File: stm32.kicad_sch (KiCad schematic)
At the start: 33 parts, among them J1 TC2030, SW1 SW_Push, U1 STM32F411CEUx, U2 BMI088, U3 BMP388, U4 W25Q128JVSIQ, Y1 Crystal_GND24

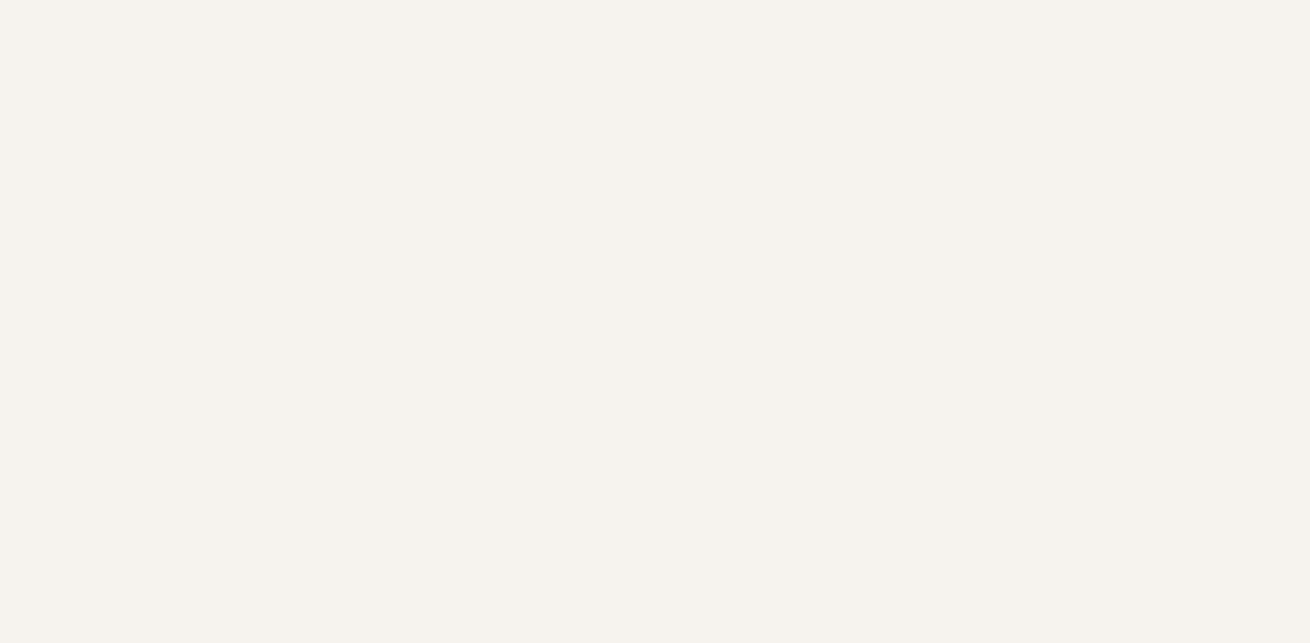
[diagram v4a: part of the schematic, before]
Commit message: Power: TP4056 charger (Iprog=255mA via 4.7k PROG, status LEDs, NTC disabled)
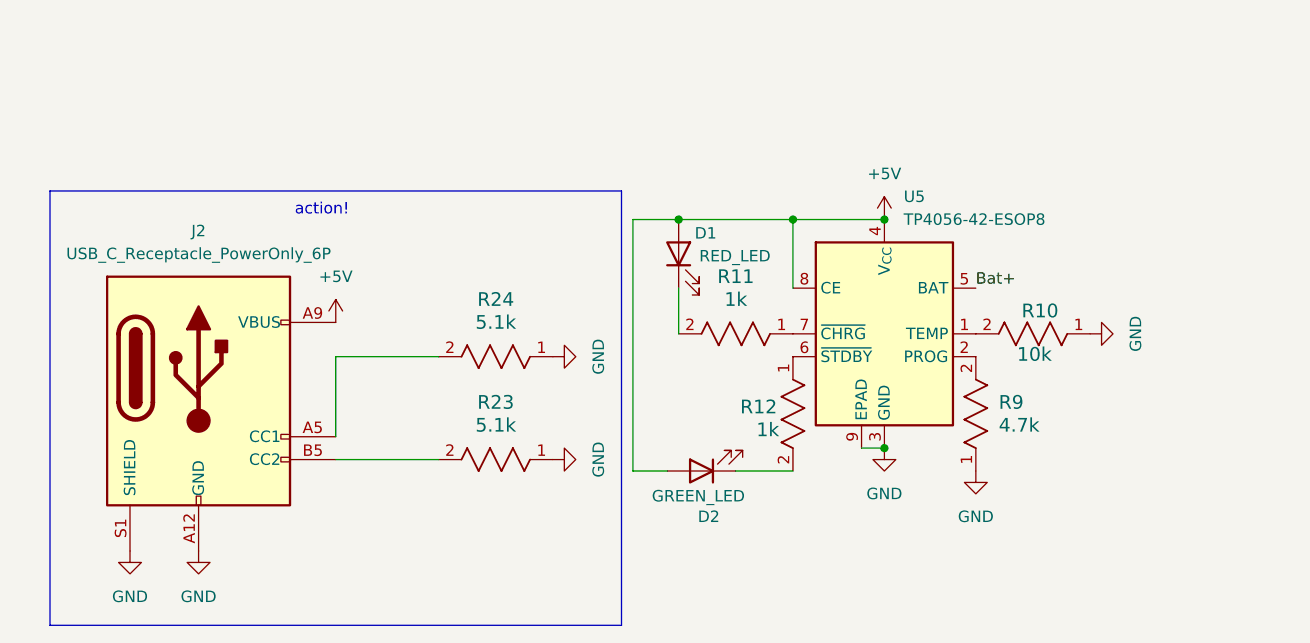
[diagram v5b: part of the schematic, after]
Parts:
- added D1: RED_LED, symbol Device:LED
- added D2: GREEN_LED, symbol Device:LED
- added J2: USB_C_Receptacle_PowerOnly_6P, Connector_USB:USB_C_Receptacle_GCT_USB4125-xx-x_6P_TopMnt_Horizontal, symbol Connector:USB_C_Receptacle_PowerOnly_6P
- added R10: 10k, 240Library:STA_CF14_STP, symbol 240Library:CF14JT1K00
- added R11, R12: 1k, 240Library:STA_CF14_STP, symbol 240Library:CF14JT1K00
- added R23, R24: 5.1k, 240Library:STA_CF14_STP, symbol 240Library:CF14JT1K00
- added R9: 4.7k, 240Library:STA_CF14_STP, symbol 240Library:CF14JT1K00
- added U5: TP4056-42-ESOP8, Package_SO:SOIC-8-1EP_3.9x4.9mm_P1.27mm_EP2.41x3.3mm_ThermalVias, symbol Battery_Management:TP4056-42-ESOP8
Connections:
- net GND: now also J2.A12 (GND), J2.B12 (GND), J2.S1 (SHIELD), R10.1, R23.1, R24.1, R9.1, U5.3 (GND), U5.9 (EPAD)
- new net: R10.2, U5.1 (TEMP)
- new net: R9.2, U5.2 (PROG)
- new net: R12.1, U5.6 (~{STDBY})
- new net: R11.1, U5.7 (~{CHRG})
- new net: D1.1 (K), R11.2
- new net: J2.A5 (CC1), R24.2
- new net: D2.1 (K), R12.2
- new net: J2.B5 (CC2), R23.2
- new net +5V: D1.2 (A), D2.2 (A), J2.A9 (VBUS), J2.B9 (VBUS), U5.4 (V_{CC}), U5.8 (CE)
- new net Bat+: U5.5 (BAT)
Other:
- note added: "action!"

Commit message: small update
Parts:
- added U6: AP63203WU, Package_TO_SOT_SMD:TSOT-23-6, symbol Regulator_Switching:AP63203WU
- R10, R11, R12, R23, R24, R9: footprint 240Library:STA_CF14_STP -> Resistor_SMD:R_0402_1005Metric
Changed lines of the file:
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@@
 	)
 	(symbol
+		(lib_id "Regulator_Switching:AP63203WU")
+		(at 180.34 123.19 0)
+		(unit 1)
+		(exclude_from_sim no)
+		(in_bom yes)
+		(on_board yes)
+		(dnp no)
+		(fields_autoplaced yes)
+		(property "Reference" "U6"
+			(at 180.34 113.03 0)
+			(effects
+				(font
+					(size 1.27 1.27)
+				)
+			)
+		)
+		(property "Value" "AP63203WU"
+			(at 180.34 115.57 0)
+			(effects
+				(font
+					(size 1.27 1.27)
+				)
+			)
+		)
+		(property "Footprint" "Package_TO_SOT_SMD:TSOT-23-6"
+			(at 180.34 146.05 0)
+			(effects
+				(font
+					(size 1.27 1.27)
+				)
+				(hide yes)
+			)
+		)
+		(property "Datasheet" "https://www.diodes.com/assets/Datasheets/AP63200-AP63201-AP63203-AP63205.pdf"
+			(at 180.34 123.19 0)
+			(effects
+				(font
+					(size 1.27 1.27)
+				)
+				(hide yes)
+			)
+		)
+		(property "Description" "2A, 1.1MHz Buck DC/DC Converter, fixed 3.3V output voltage, TSOT-23-6"
+			(at 180.34 123.19 0)
+			(effects
+				(font
+					(size 1.27 1.27)
+				)
+				(hide yes)
+			)
+		)
+		(pin "1"
+		)
+		(pin "6"
+		)
+		(pin "5"
+		)
+		(pin "4"
+		)
+		(pin "2"
+		)
+		(pin "3"
+		)
+		(instances
+			(project ""
+				(path "/807257e6-524f-404b-b91f-049b9c2bdd5b"
+					(reference "U6")
+					(unit 1)
+				)
+			)
+		)
+	)
+	(symbol
 		(lib_id "power:+5V")
 		(at 46.99 161.29 0)
@@
 			)
 		)
-		(property "Footprint" "240Library:STA_CF14_STP"
+		(property "Footprint" "Resistor_SMD:R_0402_1005Metric"
 			(at 130.81 162.56 0)
 			(effects
@@
 			)
 		)
-		(property "Footprint" "240Library:STA_CF14_STP"
+		(property "Footprint" "Resistor_SMD:R_0402_1005Metric"
 			(at 118.11 177.8 0)
 			(effects
@@
 			)
 		)
-		(property "Footprint" "240Library:STA_CF14_STP"
+		(property "Footprint" "Resistor_SMD:R_0402_1005Metric"
 			(at 97.79 162.56 0)
 			(effects
@@
 			)
 		)
-		(property "Footprint" "240Library:STA_CF14_STP"
+		(property "Footprint" "Resistor_SMD:R_0402_1005Metric"
 			(at 71.12 165.1 0)
 			(effects
@@
 			)
 		)
-		(property "Footprint" "240Library:STA_CF14_STP"
+		(property "Footprint" "Resistor_SMD:R_0402_1005Metric"
 			(at 97.79 165.1 0)
 			(effects
@@
 			)
 		)
-		(property "Footprint" "240Library:STA_CF14_STP"
+		(property "Footprint" "Resistor_SMD:R_0402_1005Metric"
 			(at 71.12 176.53 0)
 			(effects

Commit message: replaced buck
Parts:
- removed U6: AP63203WU, Package_TO_SOT_SMD:TSOT-23-6, symbol Regulator_Switching:AP63203WU
- added C19: 1u, Capacitor_SMD:C_0402_1005Metric, symbol Device:C
- added IC1: LTC3621EMS8E-3.3#PBF, SOP65P490X110-9N, symbol 2026-04-12_18-39-20:LTC3621EMS8E-3.3#PBF
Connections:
- net +3.3V: now also IC1.1 (SW), IC1.5 (FB)
- net GND: now also C19.1, IC1.8 (SGND), IC1.9 (GND)
- new net: C19.2, IC1.6 (INTVCC)
- new net VIN_BUCK: IC1.2 (VIN), IC1.3 (RUN)
- no-connect marks 3 -> 4

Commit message: fleshed out buck
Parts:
- added C20: 10u, Capacitor_SMD:C_0603_1608Metric, symbol Device:C
- added C21: 22u, Capacitor_SMD:C_0603_1608Metric, symbol Device:C
- added L1: 4.7u, Inductor_SMD:L_Coilcraft_XxL4020, symbol Device:L
- D1, D2: footprint (none) -> LED_SMD:LED_Kingbright_KPBD-3224
- IC1: footprint SOP65P490X110-9N -> Custom_Library:LTC3621EMS8E-3.3#PBF
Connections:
- net +3.3V: now also C21.2, L1.1; no longer IC1.1 (SW)
- net GND: now also C20.2, C21.1
- net VIN_BUCK: now also C20.1
- net at C19.2, IC1.6 (INTVCC): now also IC1.7 (MODE/SYNC)
- new net: IC1.1 (SW), L1.2
